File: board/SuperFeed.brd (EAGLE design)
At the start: 59.7 x 97.8 mm, 15 parts

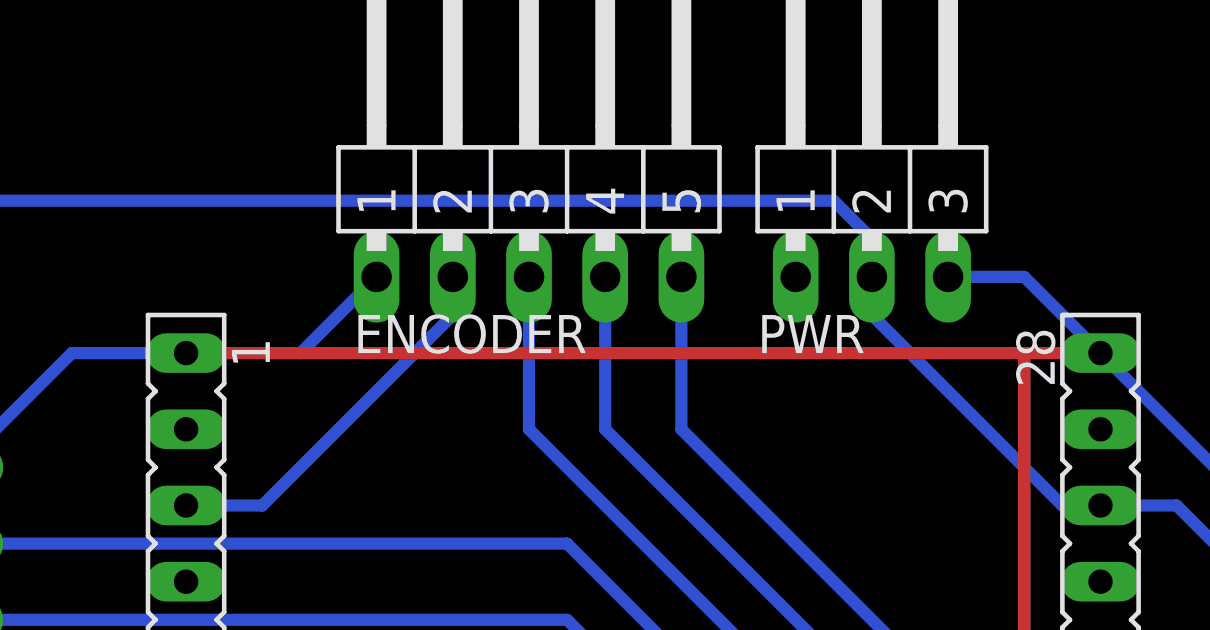
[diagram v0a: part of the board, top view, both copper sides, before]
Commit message: Connect third pin to ground on power connector
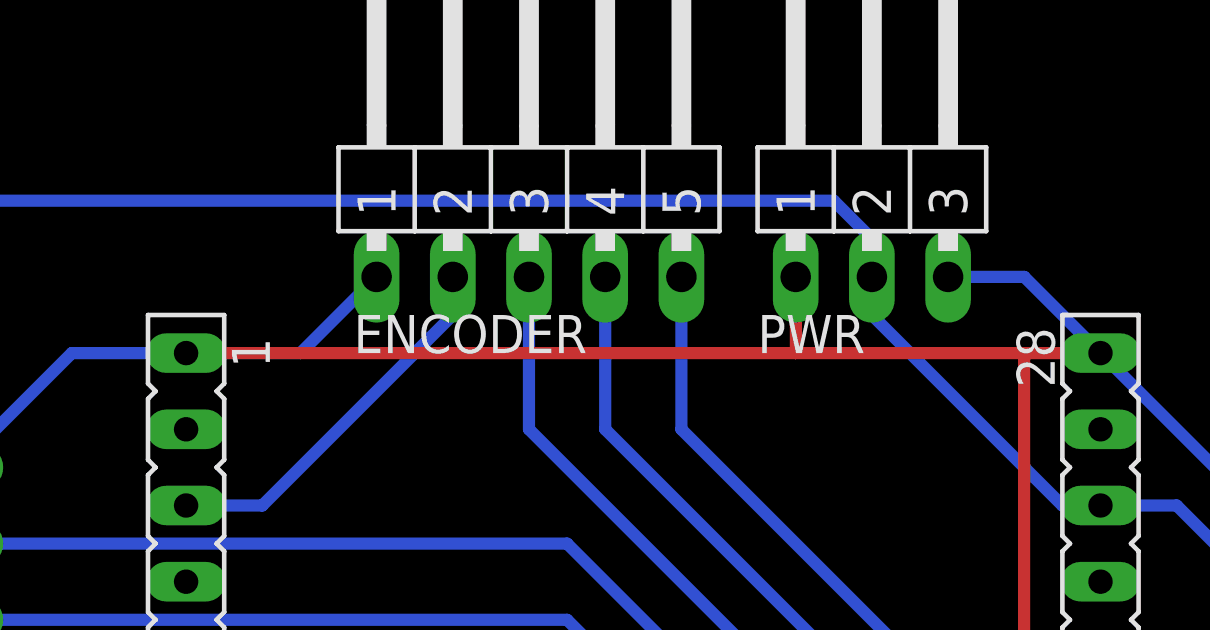
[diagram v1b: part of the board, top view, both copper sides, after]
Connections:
- net GND: now also PWR.1
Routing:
- net GND: track 252.7 -> 255.2 mm
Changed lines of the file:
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@@
 <wire x1="12.7" y1="10.16" x2="11.43" y2="11.43" width="0.4064" layer="16"/>
 <wire x1="16.51" y1="10.16" x2="44.45" y2="10.16" width="0.4064" layer="1"/>
-<wire x1="16.51" y1="78.74" x2="44.45" y2="78.74" width="0.4064" layer="1"/>
+<wire x1="16.51" y1="78.74" x2="36.83" y2="78.74" width="0.4064" layer="1"/>
+<wire x1="36.83" y1="78.74" x2="44.45" y2="78.74" width="0.4064" layer="1"/>
 <wire x1="44.45" y1="78.74" x2="44.45" y2="21.59" width="0.4064" layer="1"/>
 <wire x1="59.69" y1="66.04" x2="46.99" y2="78.74" width="0.4064" layer="16"/>
@@
 <wire x1="44.45" y1="10.16" x2="44.45" y2="21.59" width="0.4064" layer="1"/>
 <wire x1="46.99" y1="78.74" x2="44.45" y2="78.74" width="0.4064" layer="1"/>
+<contactref element="PWR" pad="1"/>
+<wire x1="36.83" y1="81.28" x2="36.83" y2="78.74" width="0.4064" layer="1"/>
 </signal>
 <signal name="+5V">

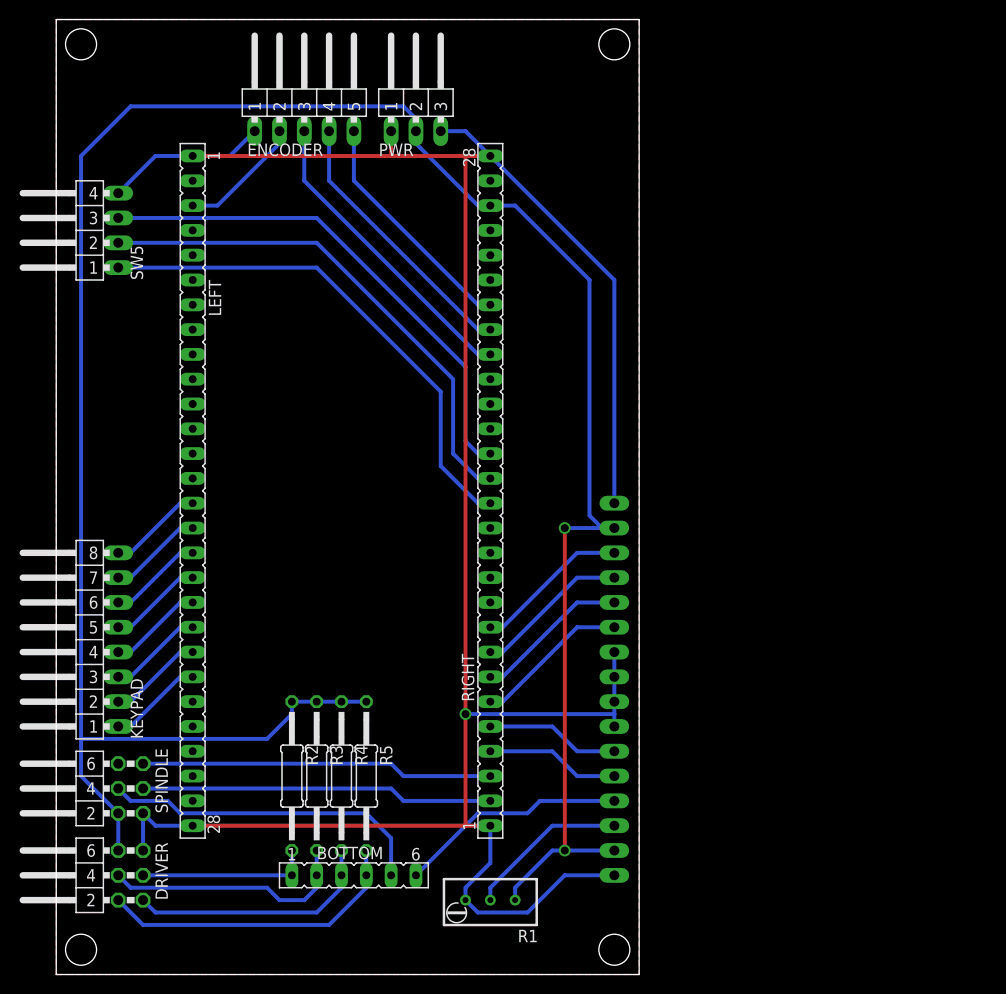
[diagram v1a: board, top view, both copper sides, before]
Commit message: Rotating board to fit into 80x100mm limitation
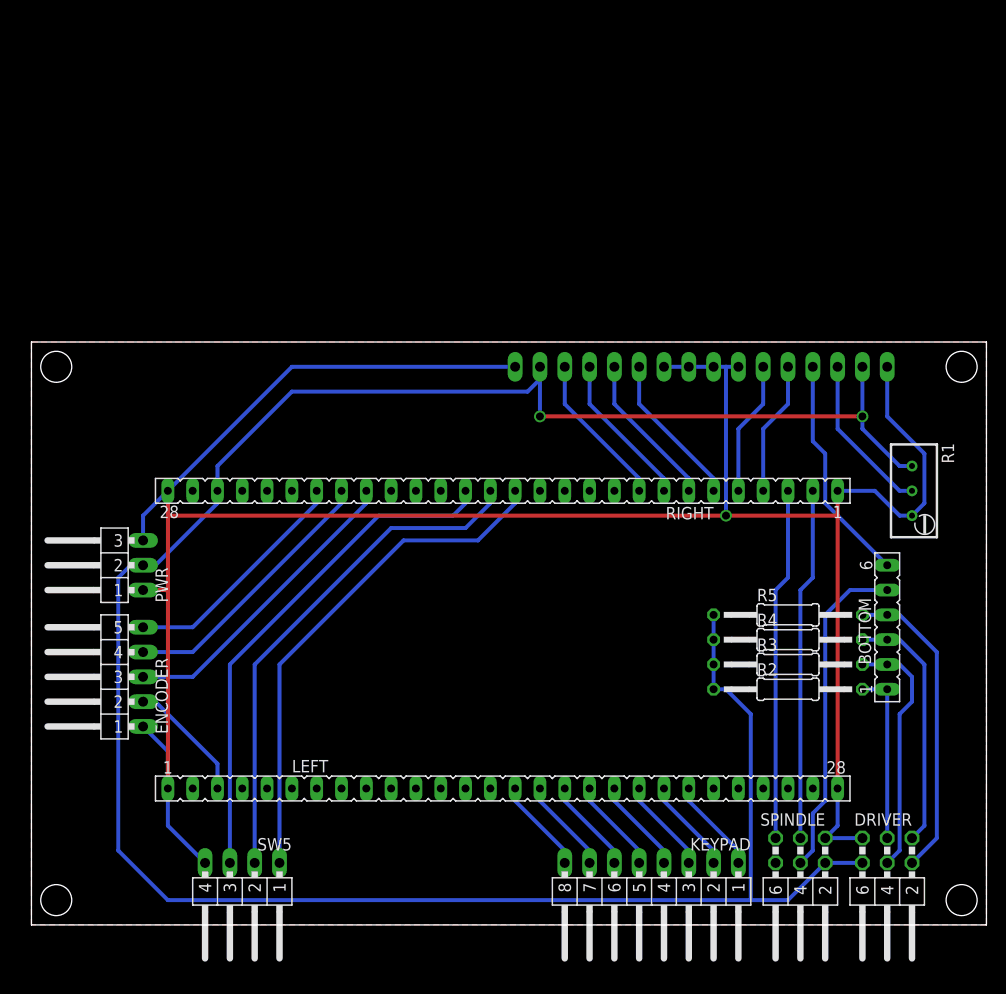
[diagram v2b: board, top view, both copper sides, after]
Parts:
- moved DRIVER 77.5 mm to (87.6, 7.62), turned to 180 degrees
- moved SPINDLE 68.9 mm to (78.7, 7.62), turned to 180 degrees
- moved SW5 66.0 mm to (21.6, 6.35), turned to 180 degrees
- moved BOTTOM 60.2 mm to (87.6, 30.5), turned to 90 degrees
- moved R1 60.2 mm to (90.2, 44.5), turned to 180 degrees
- moved KEYPAD 59.2 mm to (63.5, 6.35), turned to 180 degrees
- moved ENCODER 58.3 mm to (11.4, 25.4), turned to 90 degrees
- moved PWR 52.5 mm to (11.4, 36.8), turned to 90 degrees
- moved R2 51.6 mm to (77.5, 24.1), turned to 0 degrees
- moved R3 49.6 mm to (77.5, 26.7), turned to 0 degrees
- moved R4 47.8 mm to (77.5, 29.2), turned to 0 degrees
- moved R5 46.2 mm to (77.5, 31.8), turned to 0 degrees
- moved LEFT 44.0 mm to (48.3, 14.0), turned to 0 degrees
- moved LCD 34.2 mm to (68.6, 57.1), turned to 0 degrees
- moved RIGHT 1.27 mm to (48.3, 44.5), turned to 180 degrees
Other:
- board size 59.7 x 97.8 mm -> 97.8 x 59.7 mm

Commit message: Adding extra buttons on board
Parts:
- added EXTBTN: (no value), SuperFeed:MA05-1W
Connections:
- net GND: now also EXTBTN.5
- net PB8: now also LCD.5
- net PB9: now also LCD.6
- net PC0: now also EXTBTN.4
- net PC1: now also EXTBTN.3
- net PC2: now also EXTBTN.2
- net PC3: now also EXTBTN.1
- net PC8: no longer LCD.5
- net PC9: no longer LCD.6
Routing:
- net PB8: track 0.00 -> 64.6 mm, vias 0 -> 2
- net PB9: track 0.00 -> 63.8 mm, vias 0 -> 2
- net GND: track 255.2 -> 277.1 mm
- net PC9: track 13.8 -> 0.00 mm
- net PC8: track 13.8 -> 0.00 mm
- net PC3: track 0.00 -> 7.62 mm
- net PC2: track 0.00 -> 7.62 mm
- net PC1: track 0.00 -> 7.62 mm
- net PC0: track 0.00 -> 7.62 mm
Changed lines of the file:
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@@
 <grid distance="0.05" unitdist="inch" unit="inch" style="dots" multiple="1" display="yes" altdistance="0.025" altunitdist="inch" altunit="inch"/>
 <layers>
-<layer number="1" name="Top" color="4" fill="1" visible="yes" active="yes"/>
+<layer number="1" name="Top" color="4" fill="1" visible="no" active="yes"/>
 <layer number="2" name="Route2" color="1" fill="3" visible="no" active="no"/>
 <layer number="15" name="Route15" color="4" fill="6" visible="no" active="no"/>
@@
 <layer number="27" name="tValues" color="7" fill="1" visible="yes" active="yes"/>
 <layer number="28" name="bValues" color="7" fill="1" visible="yes" active="yes"/>
-<layer number="29" name="tStop" color="7" fill="3" visible="yes" active="yes"/>
-<layer number="30" name="bStop" color="7" fill="6" visible="yes" active="yes"/>
+<layer number="29" name="tStop" color="7" fill="3" visible="no" active="yes"/>
+<layer number="30" name="bStop" color="7" fill="6" visible="no" active="yes"/>
 <layer number="31" name="tCream" color="7" fill="4" visible="yes" active="yes"/>
 <layer number="32" name="bCream" color="7" fill="5" visible="yes" active="yes"/>
@@
 <layer number="42" name="bRestrict" color="1" fill="10" visible="yes" active="yes"/>
 <layer number="43" name="vRestrict" color="2" fill="10" visible="yes" active="yes"/>
-<layer number="44" name="Drills" color="7" fill="1" visible="yes" active="yes"/>
-<layer number="45" name="Holes" color="7" fill="1" visible="yes" active="yes"/>
+<layer number="44" name="Drills" color="7" fill="1" visible="no" active="yes"/>
+<layer number="45" name="Holes" color="7" fill="1" visible="no" active="yes"/>
 <layer number="46" name="Milling" color="3" fill="1" visible="yes" active="yes"/>
 <layer number="47" name="Measures" color="7" fill="1" visible="yes" active="yes"/>
@@
 <element name="R4" library="SuperFeed" package="0207/15" value="10k" x="77.47" y="29.21"/>
 <element name="R5" library="SuperFeed" package="0207/15" value="10k" x="77.47" y="31.75"/>
+<element name="EXTBTN" library="SuperFeed" package="MA05-1W" value="" x="41.91" y="6.35" rot="R180"/>
 </elements>
 <signals>
@@
 <contactref element="PWR" pad="1"/>
 <wire x1="11.43" y1="34.29" x2="13.97" y2="34.29" width="0.4064" layer="1"/>
+<contactref element="EXTBTN" pad="5"/>
+<wire x1="34.29" y1="3.81" x2="36.83" y2="6.35" width="0.4064" layer="16"/>
+<wire x1="17.78" y1="6.35" x2="17.78" y2="5.08" width="0.4064" layer="16"/>
+<wire x1="17.78" y1="5.08" x2="19.05" y2="3.81" width="0.4064" layer="16"/>
+<wire x1="19.05" y1="3.81" x2="34.29" y2="3.81" width="0.4064" layer="16"/>
 </signal>
 <signal name="+5V">
@@
 <signal name="PB9">
 <contactref element="RIGHT" pad="25"/>
+<contactref element="LCD" pad="6"/>
+<wire x1="74.93" y1="57.15" x2="74.93" y2="50.8" width="0.4064" layer="16"/>
+<via x="74.93" y="50.8" extent="1-16" drill="0.8128"/>
+<wire x1="74.93" y1="50.8" x2="25.4" y2="50.8" width="0.4064" layer="1"/>
+<wire x1="25.4" y1="50.8" x2="21.59" y2="46.99" width="0.4064" layer="1"/>
+<via x="21.59" y="46.99" extent="1-16" drill="0.8128"/>
+<wire x1="21.59" y1="46.99" x2="21.59" y2="44.45" width="0.4064" layer="16"/>
 </signal>
 <signal name="PB8">
 <contactref element="RIGHT" pad="24"/>
+<contactref element="LCD" pad="5"/>
+<wire x1="77.47" y1="57.15" x2="77.47" y2="49.53" width="0.4064" layer="16"/>
+<via x="77.47" y="49.53" extent="1-16" drill="0.8128"/>
+<wire x1="77.47" y1="49.53" x2="26.67" y2="49.53" width="0.4064" layer="1"/>
+<wire x1="26.67" y1="49.53" x2="24.13" y2="46.99" width="0.4064" layer="1"/>
+<via x="24.13" y="46.99" extent="1-16" drill="0.8128"/>
+<wire x1="24.13" y1="46.99" x2="24.13" y2="44.45" width="0.4064" layer="16"/>
 </signal>
 <signal name="BOOT">
@@
 <signal name="PC9">
 <contactref element="RIGHT" pad="5"/>
-<contactref element="LCD" pad="6"/>
-<wire x1="74.93" y1="57.15" x2="74.93" y2="53.34" width="0.4064" layer="16"/>
-<wire x1="74.93" y1="53.34" x2="72.39" y2="50.8" width="0.4064" layer="16"/>
-<wire x1="72.39" y1="50.8" x2="72.39" y2="44.45" width="0.4064" layer="16"/>
 </signal>
 <signal name="PC8">
 <contactref element="RIGHT" pad="4"/>
-<contactref element="LCD" pad="5"/>
-<wire x1="74.93" y1="44.45" x2="74.93" y2="50.8" width="0.4064" layer="16"/>
-<wire x1="74.93" y1="50.8" x2="77.47" y2="53.34" width="0.4064" layer="16"/>
-<wire x1="77.47" y1="53.34" x2="77.47" y2="57.15" width="0.4064" layer="16"/>
 </signal>
 <signal name="PC7">
@@
 <signal name="PC3">
 <contactref element="LEFT" pad="14"/>
+<contactref element="EXTBTN" pad="1"/>
+<wire x1="46.99" y1="6.35" x2="46.99" y2="13.97" width="0.4064" layer="16"/>
 </signal>
 <signal name="PC2">
 <contactref element="LEFT" pad="13"/>
+<contactref element="EXTBTN" pad="2"/>
+<wire x1="44.45" y1="13.97" x2="44.45" y2="6.35" width="0.4064" layer="16"/>
 </signal>
 <signal name="PC1">
 <contactref element="LEFT" pad="12"/>
+<contactref element="EXTBTN" pad="3"/>
+<wire x1="41.91" y1="13.97" x2="41.91" y2="6.35" width="0.4064" layer="16"/>
 </signal>
 <signal name="PC0">
 <contactref element="LEFT" pad="11"/>
+<contactref element="EXTBTN" pad="4"/>
+<wire x1="39.37" y1="13.97" x2="39.37" y2="6.35" width="0.4064" layer="16"/>
 </signal>
 <signal name="PA1">
